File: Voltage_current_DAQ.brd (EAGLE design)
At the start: 26 parts, among them IC1 INA128U

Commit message: updated the initial layout
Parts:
- moved LOGO1 44.7 mm to (6.39, 4.27)
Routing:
- net N$14: track 7.85 -> 40.8 mm, vias 0 -> 1
- net N$1: track 16.5 -> 30.4 mm, vias 0 -> 2
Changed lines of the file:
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@@
 </element>
 <element name="U$1" library="SparkFun-AnalogIC" package="SO08" value="LM393" x="11.6" y="11.38"/>
-<element name="R3" library="rcl" package="R0603" value="" x="10.908" y="5.59" rot="R180"/>
+<element name="R3" library="rcl" package="R0603" value="" x="10.908" y="5.59" smashed="yes" rot="R180">
+<attribute name="NAME" x="12.051" y="7.495" size="1.27" layer="25" rot="R180"/>
+<attribute name="VALUE" x="11.543" y="7.495" size="1.27" layer="27" rot="R180"/>
+</element>
 <element name="R4" library="rcl" package="R0603" value="" x="20.4" y="6.4" rot="R180"/>
 <element name="R5" library="rcl" package="RTRIM64Y" value="" x="23.68" y="23.004" rot="R270"/>
-<element name="C1" library="rcl" package="C0805" value="" x="16.29" y="6.48" rot="R180"/>
+<element name="C1" library="rcl" package="C0805" value="" x="16.29" y="6.48" smashed="yes" rot="R180">
+<attribute name="NAME" x="17.56" y="8.766" size="1.27" layer="25" rot="R180"/>
+<attribute name="VALUE" x="17.56" y="9.02" size="1.27" layer="27" rot="R180"/>
+</element>
 <element name="C2" library="rcl" package="C0805" value="" x="26.71" y="3.44"/>
 <element name="C3" library="rcl" package="C0805" value="" x="7.49" y="17.934"/>
@@
 </element>
 <element name="R9" library="rcl" package="R0603" value="" x="26.258" y="14.606" rot="R180"/>
-<element name="LOGO1" library="SparkFun-Aesthetics" package="OSHW-LOGO-L" value="OSHW-LOGOL" x="49.828" y="14.938"/>
+<element name="LOGO1" library="SparkFun-Aesthetics" package="OSHW-LOGO-L" value="OSHW-LOGOL" x="6.394" y="4.27"/>
 <element name="H5" library="holes" package="3,0-PAD" value="MOUNT-PAD-ROUND3.0" x="0" y="27"/>
 <element name="H1" library="holes" package="3,0-PAD" value="MOUNT-PAD-ROUND3.0" x="33" y="27"/>
@@
 <wire x1="27.178" y1="7.874" x2="27.66" y2="7.392" width="0.4064" layer="1"/>
 <wire x1="27.66" y1="7.392" x2="27.66" y2="3.44" width="0.4064" layer="1"/>
-<wire x1="11.758" y1="5.59" x2="19.558" y2="10.7368" width="0" layer="19" extent="1-1"/>
+<wire x1="11.758" y1="5.59" x2="11.938" y2="5.41" width="0.4064" layer="1"/>
+<wire x1="11.938" y1="5.41" x2="11.938" y2="3.81" width="0.4064" layer="1"/>
+<via x="11.938" y="3.81" extent="1-16" drill="0.6" shape="square"/>
+<wire x1="11.938" y1="3.81" x2="14.478" y2="6.35" width="0.4064" layer="16"/>
+<wire x1="14.478" y1="6.35" x2="17.78" y2="6.35" width="0.4064" layer="16"/>
+<wire x1="17.78" y1="6.35" x2="19.558" y2="8.128" width="0.4064" layer="16"/>
+<wire x1="19.558" y1="8.128" x2="19.558" y2="8.636" width="0.4064" layer="16"/>
+<via x="19.558" y="8.636" extent="1-16" drill="0.6" shape="square"/>
+<wire x1="19.558" y1="8.636" x2="19.585" y2="8.663" width="0.4064" layer="1"/>
+<wire x1="19.585" y1="8.663" x2="19.585" y2="10.7638" width="0.4064" layer="1"/>
 </signal>
 <signal name="N$2">
@@
 <contactref element="C7" pad="1"/>
 <contactref element="C8" pad="1"/>
-<wire x1="10.542" y1="16.46" x2="10.542" y2="15.62" width="0.4064" layer="1"/>
-<wire x1="10.542" y1="15.62" x2="10.922" y2="15.24" width="0.4064" layer="1"/>
 <wire x1="10.922" y1="14.0392" x2="10.965" y2="13.9962" width="0.4064" layer="1"/>
 <wire x1="10.558" y1="20.238" x2="10.558" y2="18.464" width="0.4064" layer="1"/>
 <wire x1="10.558" y1="18.464" x2="10.8" y2="18.222" width="0.4064" layer="1"/>
-<wire x1="10.922" y1="15.24" x2="10.922" y2="18.1" width="0.4064" layer="1"/>
-<wire x1="10.922" y1="18.1" x2="10.8" y2="18.222" width="0.4064" layer="1"/>
-<wire x1="10.922" y1="15.24" x2="10.965" y2="15.197" width="0.4064" layer="1"/>
-<wire x1="10.965" y1="15.197" x2="10.965" y2="13.9962" width="0.4064" layer="1"/>
-<wire x1="10.965" y1="15.197" x2="31" y2="15.27" width="0" layer="19" extent="1-1"/>
+<wire x1="10.8" y1="18.222" x2="10.542" y2="17.964" width="0.4064" layer="1"/>
+<wire x1="10.542" y1="17.964" x2="10.542" y2="16.46" width="0.4064" layer="1"/>
+<wire x1="10.542" y1="16.46" x2="10.668" y2="16.334" width="0.4064" layer="1"/>
+<wire x1="10.965" y1="16.037" x2="10.965" y2="13.9962" width="0.4064" layer="1"/>
+<wire x1="10.965" y1="16.037" x2="10.668" y2="16.334" width="0.4064" layer="1"/>
+<wire x1="10.668" y1="16.334" x2="10.668" y2="21.336" width="0.4064" layer="1"/>
+<via x="10.668" y="21.336" extent="1-16" drill="0.6" shape="square"/>
+<wire x1="10.668" y1="21.336" x2="13.716" y2="24.384" width="0.4064" layer="16"/>
+<wire x1="13.716" y1="24.384" x2="27.178" y2="24.384" width="0.4064" layer="16"/>
+<wire x1="27.178" y1="24.384" x2="28.702" y2="22.86" width="0.4064" layer="16"/>
+<wire x1="28.702" y1="22.86" x2="28.702" y2="16.51" width="0.4064" layer="16"/>
+<wire x1="28.702" y1="16.51" x2="29.942" y2="15.27" width="0.4064" layer="16"/>
+<wire x1="29.942" y1="15.27" x2="31" y2="15.27" width="0.4064" layer="16"/>
 </signal>
 <signal name="N$15">
@@
 <via x="8.636" y="16.002" extent="1-16" drill="0.6" shape="square"/>
 <wire x1="8.636" y1="16.002" x2="9.144" y2="16.002" width="0.4064" layer="1"/>
-<wire x1="9.144" y1="16.002" x2="9.652" y2="15.494" width="0.4064" layer="1"/>
-<wire x1="9.652" y1="15.494" x2="9.652" y2="14.0392" width="0.4064" layer="1"/>
 <wire x1="9.652" y1="14.0392" x2="9.695" y2="13.9962" width="0.4064" layer="1"/>
 <wire x1="4.856" y1="7.65" x2="2" y2="7.65" width="0.4064" layer="16"/>
@@
 <wire x1="6.604" y1="16.51" x2="7.112" y2="16.002" width="0.4064" layer="1"/>
 <wire x1="7.112" y1="16.002" x2="8.636" y2="16.002" width="0.4064" layer="1"/>
+<wire x1="9.144" y1="16.002" x2="9.695" y2="15.451" width="0.4064" layer="1"/>
+<wire x1="9.695" y1="15.451" x2="9.695" y2="13.9962" width="0.4064" layer="1"/>
 <wire x1="30.97" y1="7.62" x2="31" y2="7.65" width="0" layer="19" extent="1-1"/>
 <wire x1="9.695" y1="13.9962" x2="19.585" y2="13.943" width="0" layer="19" extent="1-1"/>

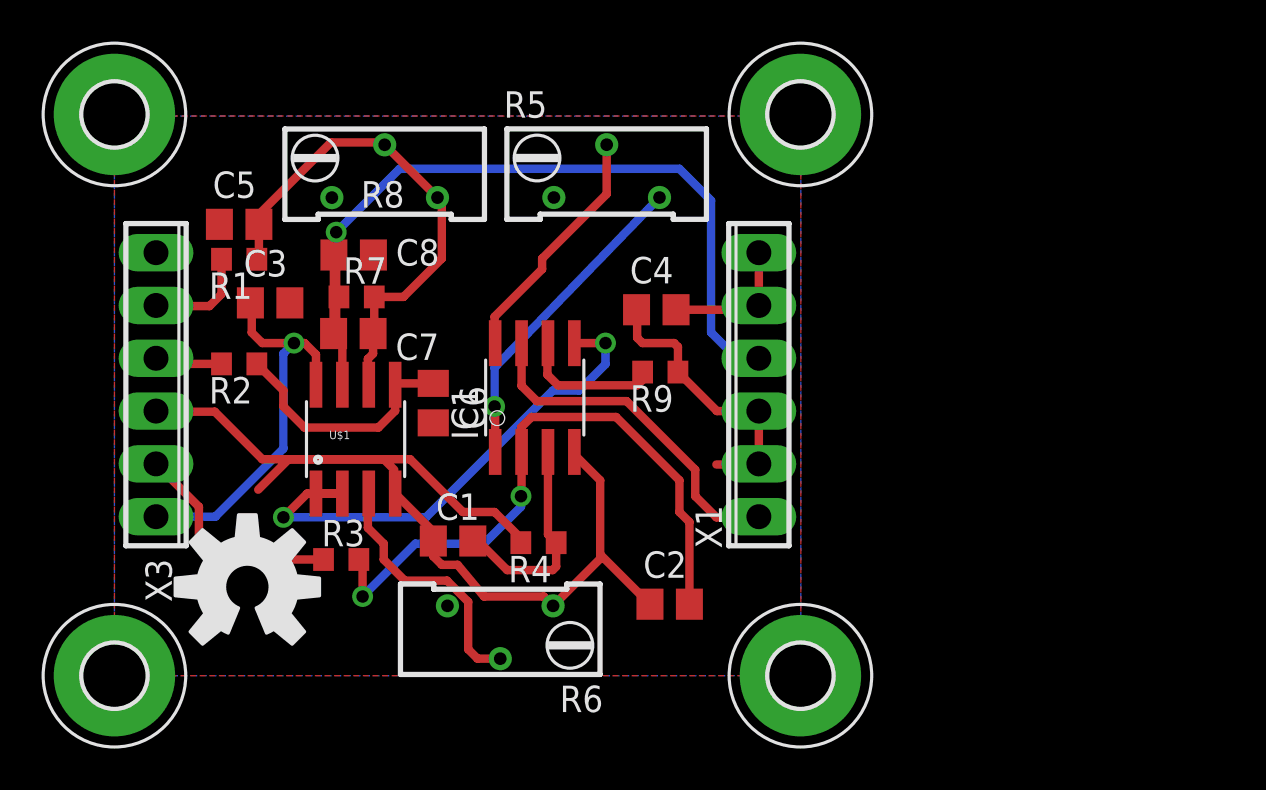
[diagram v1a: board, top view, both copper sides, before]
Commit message: gerbers generated sent to OSHpark
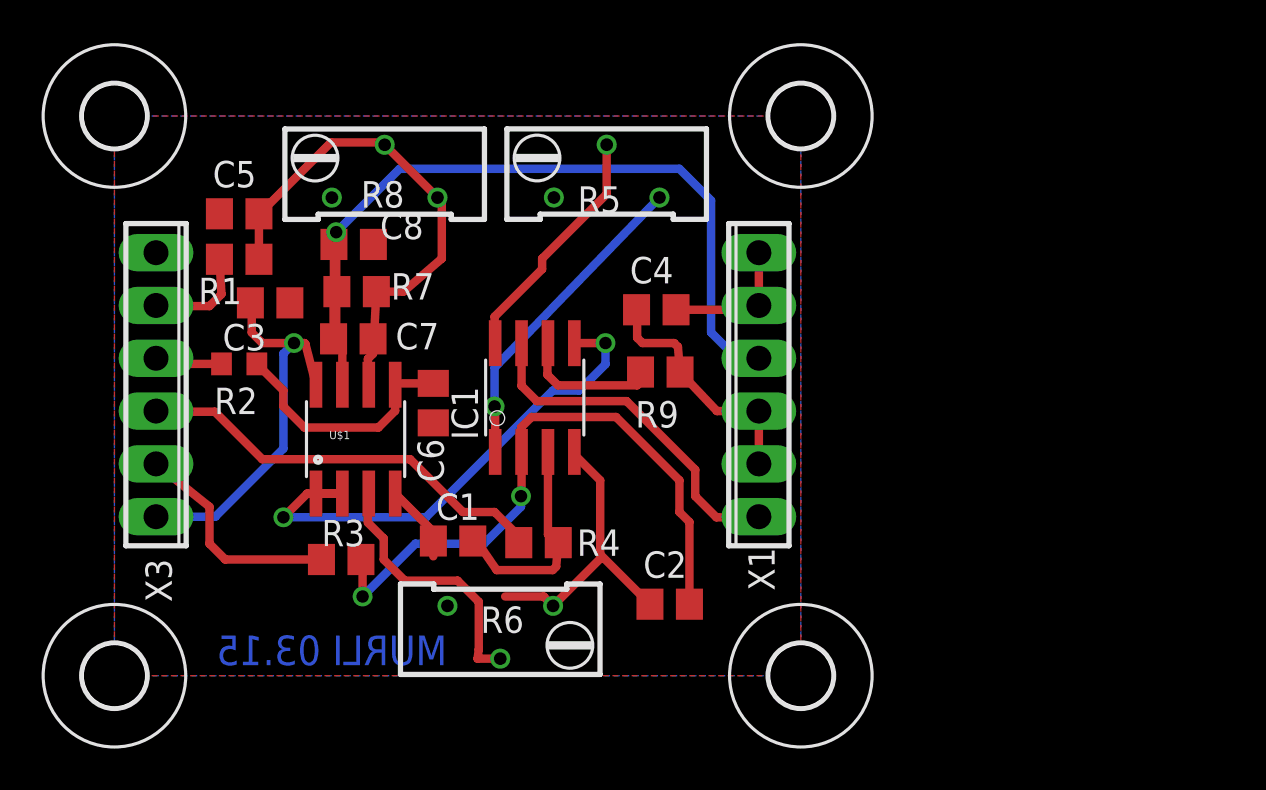
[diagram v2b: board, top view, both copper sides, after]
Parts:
- removed H5: MOUNT-PAD-ROUND3.0, holes:3,0-PAD
- added H4: MOUNT-HOLE3.0, holes:3,0
- H1, H2, H3: value MOUNT-PAD-ROUND3.0 -> MOUNT-HOLE3.0; device holes:3,0-PAD -> holes:3,0
- R1, R3, R4, R7, R9: device rcl:R0603 -> rcl:R0805
- moved H3 33.0 mm to (33.0, 0.00)
- moved H1 33.0 mm to (0.00, 26.9)
- moved H2 26.9 mm to (33.0, 26.9)
- moved C5 0.51 mm to (6.00, 22.2)
- moved C8 0.51 mm to (11.5, 20.7)
- moved C7 0.25 mm to (11.5, 16.2)
- moved LOGO1 0.25 mm to (6.39, 4.02), flipped to the bottom
- moved R7 0.25 mm to (11.7, 18.5)
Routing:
- net GND: track 36.8 -> 25.1 mm
- net N$8: track 14.0 -> 11.9 mm
- net N$14: track 40.8 -> 41.5 mm
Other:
- board text added: "MURLI 03.15"
